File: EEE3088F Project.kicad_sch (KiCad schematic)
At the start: 69 parts, among them J1 Conn_02x16_Odd_Even, J2 Battery IN JST, M1Control1 DRV8837, M2Control1 DRV8837, M3Control1 DRV8837, M4Control1 DRV8837, Q2 AO3400A, U1 TP4056, U2 TPS62163DSG, U3 MT3608, U5 TPS62162DSG, U6 CH224K

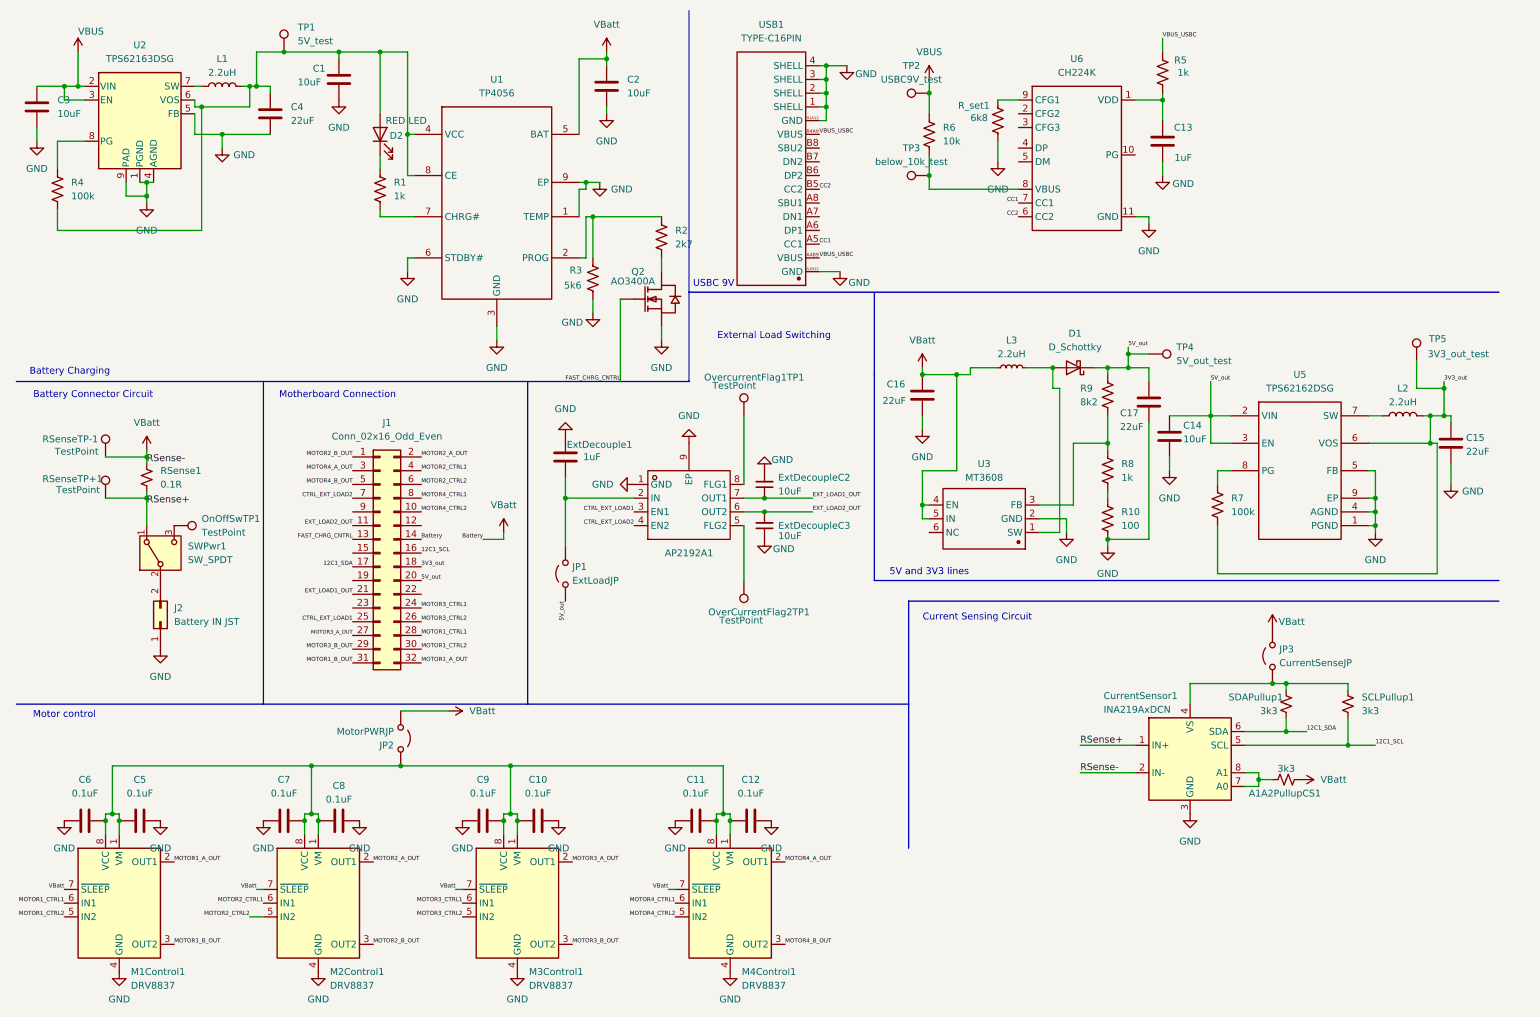
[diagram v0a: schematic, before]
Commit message: Fixed BOM
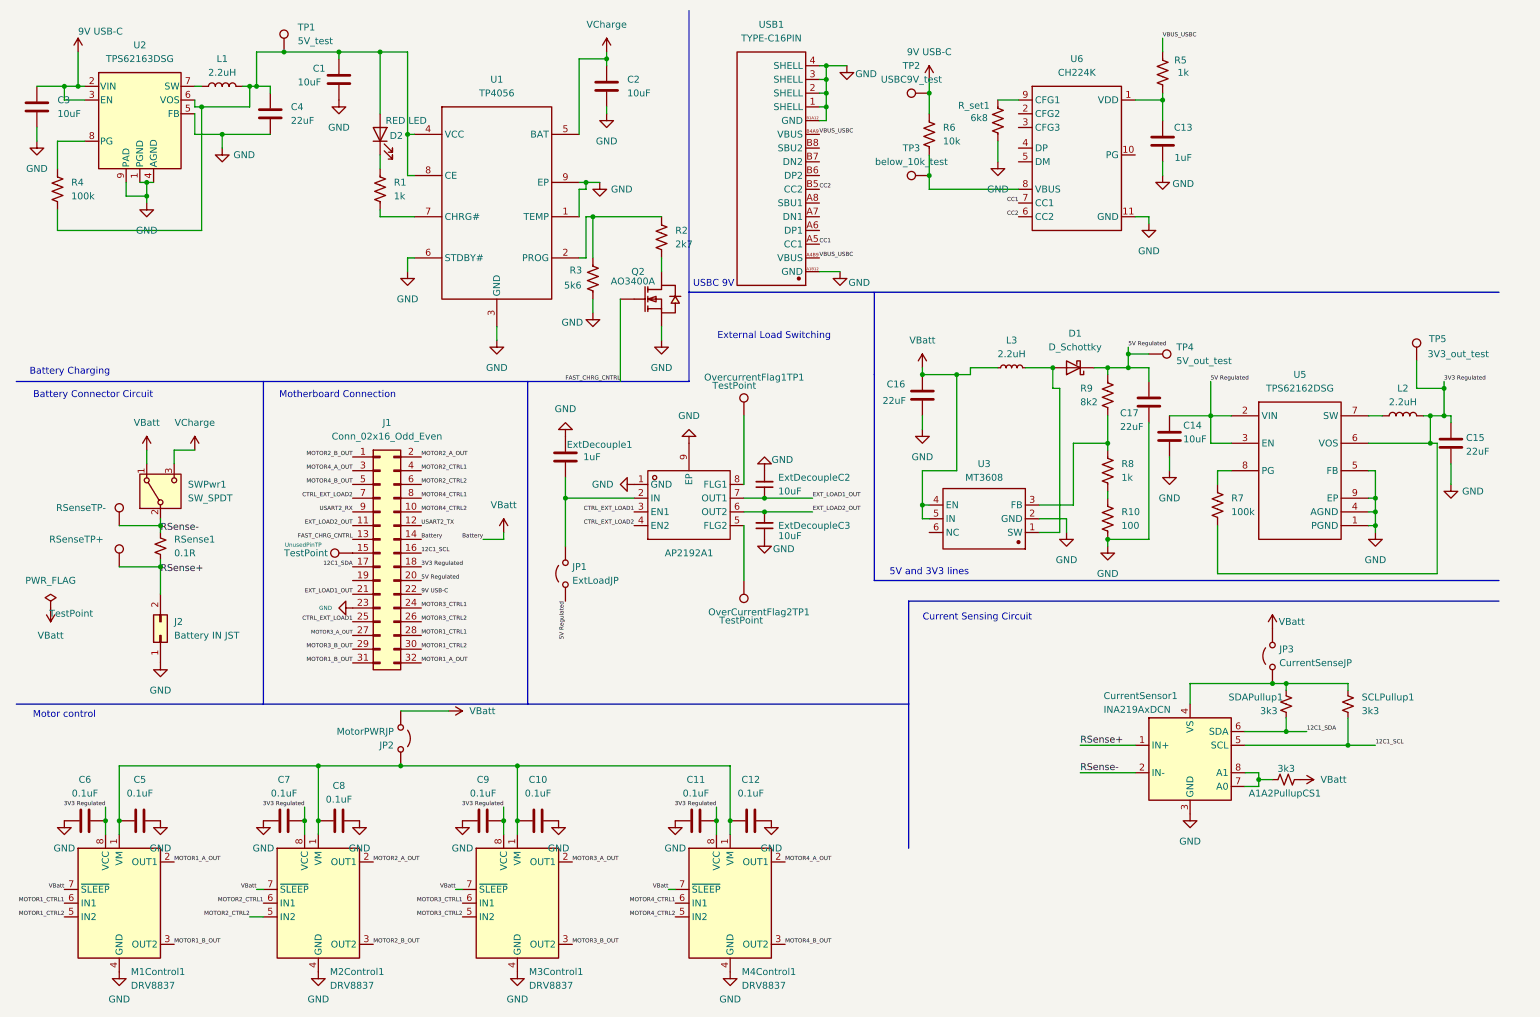
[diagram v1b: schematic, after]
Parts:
- removed OnOffSwTP1: TestPoint, symbol Connector:TestPoint
- added UnusedPinTP: TestPoint, symbol Connector:TestPoint
- renumbered RSenseTP+1 to RSenseTP+, RSenseTP-1 to RSenseTP-
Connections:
- net VBUS is gone; now on net 9V USB-C: C3.1, R6.1, TP2.1, U2.2 (VIN), U2.3 (EN)
- net GND: now also J1.23 (Pin_23)
- net RSense+: now also J2.2 (Pin_2); no longer SWPwr1.1 (A)
- net VBatt: now also SWPwr1.1 (A); no longer C2.1, CurrentSensor1.2 (IN-), RSense1.1, RSenseTP-.1, U1.5 (BAT)
- net USART2_TX: now reaches J1.12 (Pin_12)
- net at J1.15 (Pin_15): now also UnusedPinTP.1
- net 9V USB-C: now reaches J1.22 (Pin_22)
- net USART2_RX: now reaches J1.9 (Pin_9)
- net at C10.1, C12.1, C5.1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: no longer C11.2, C6.2, C7.2, C9.2, M1Control1.8 (VCC), M2Control1.8 (VCC), M3Control1.8 (VCC), M4Control1.8 (VCC)
- net VCharge: now reaches SWPwr1.3 (C)
- net VCharge: now also C2.1, U1.5 (BAT)
- net RSense-: now reaches SWPwr1.2 (B)
- net RSense-: now also CurrentSensor1.2 (IN-), RSense1.1, RSenseTP-.1; no longer J2.2 (Pin_2)
- net 3V3_out renamed 3V3 Regulated
- net 3V3 Regulated: now also C11.2, C6.2, C7.2, C9.2, M1Control1.8 (VCC), M2Control1.8 (VCC), M3Control1.8 (VCC), M4Control1.8 (VCC)
- net 5V_out renamed 5V Regulated
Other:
- moved on the sheet: J2, RSense1, RSenseTP+, RSenseTP-, SWPwr1

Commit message: changed inductors
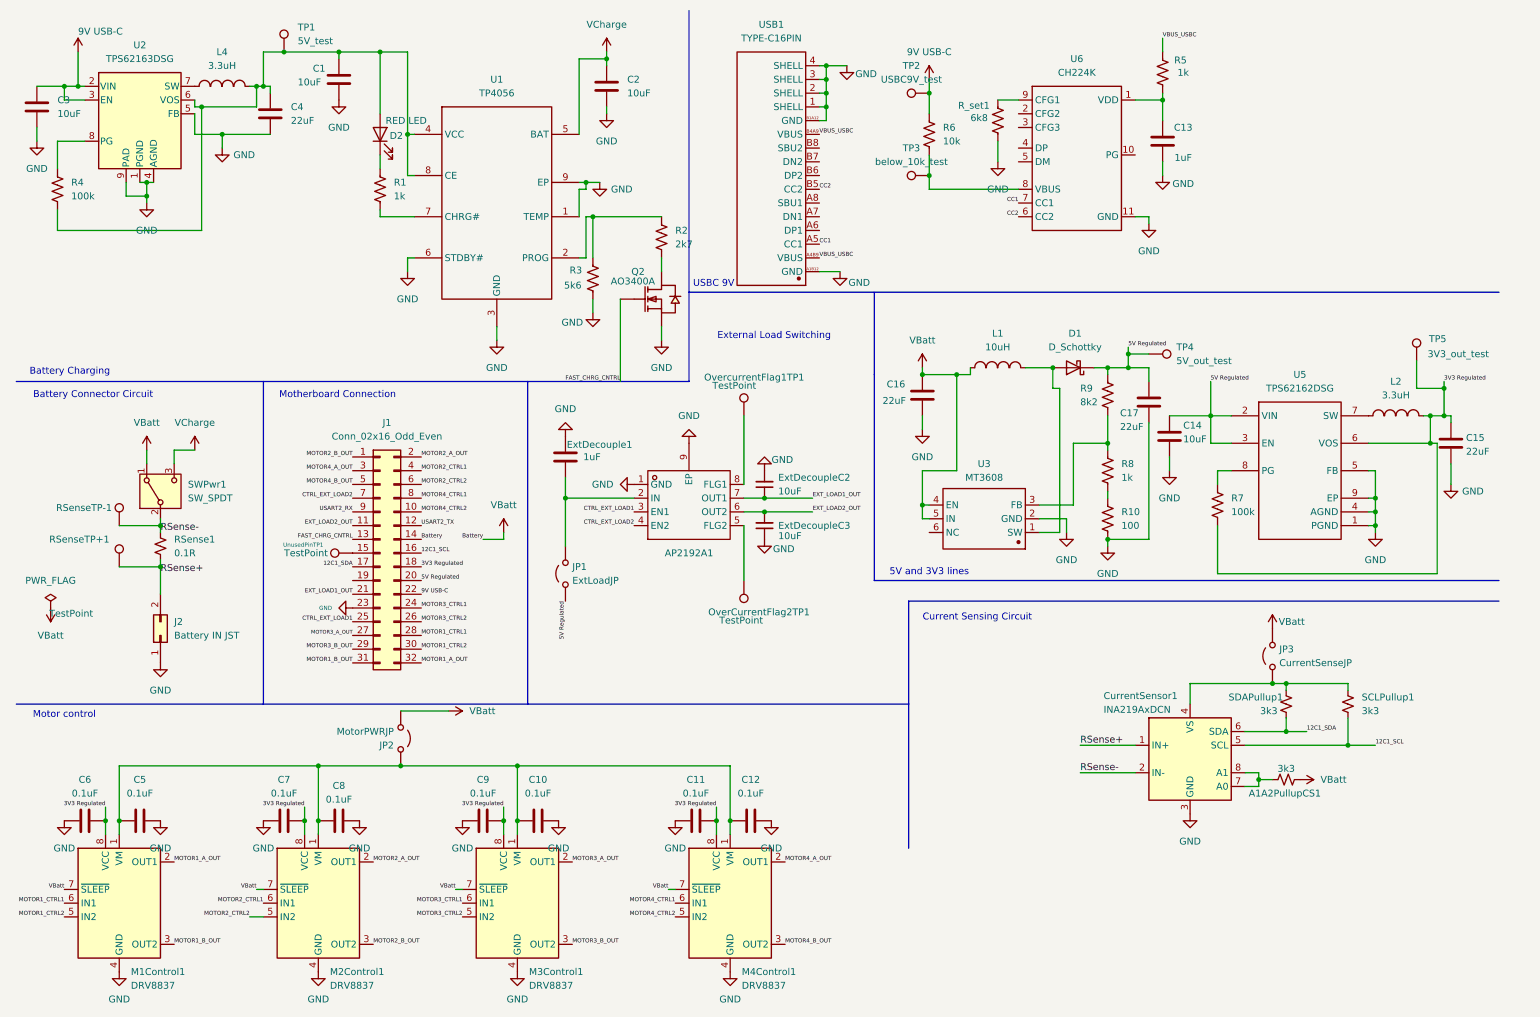
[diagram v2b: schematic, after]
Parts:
- removed L1, L2: 2.2uH, Inductor_SMD:L_Taiyo-Yuden_MD-3030, symbol Device:L
- removed L3: 2.2uH, Inductor_SMD:L_Taiyo-Yuden_MD-3030, symbol Device:L_Small
- added L1: 10uH, Custom Footprints:IND-SMD_L7.8-W7.0-A, symbol Custom Symbols:SM7850-100MT
- added L2, L4: 3.3uH, Custom Footprints:IND-SMD_L4.0-W4.0_FNR40XXS, symbol Custom Symbols:FNR4030S3R3MT
- OverCurrentFlag2TP1, OvercurrentFlag1TP1, TP1, TP2, TP3, TP4, TP5: footprint (none) -> TestPoint:TestPoint_Pad_2.0x2.0mm
- UnusedPinTP1: renamed from UnusedPinTP; footprint (none) -> TestPoint:TestPoint_Pad_2.0x2.0mm
- renumbered RSenseTP+ to RSenseTP+1, RSenseTP- to RSenseTP-1
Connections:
- net 3V3 Regulated: now also L2.2
- net VBatt: now also L1.1
- net at D1.2 (A), U3.1 (SW): now also L1.2
- net at C1.2, C4.1, D2.2 (A)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: now also L4.2
- net at U2.7 (SW): now also L4.1
- net at U5.7 (SW): now also L2.1

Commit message: Routed Thomas half of PCB traces. Minor labelling modifications in schematic.
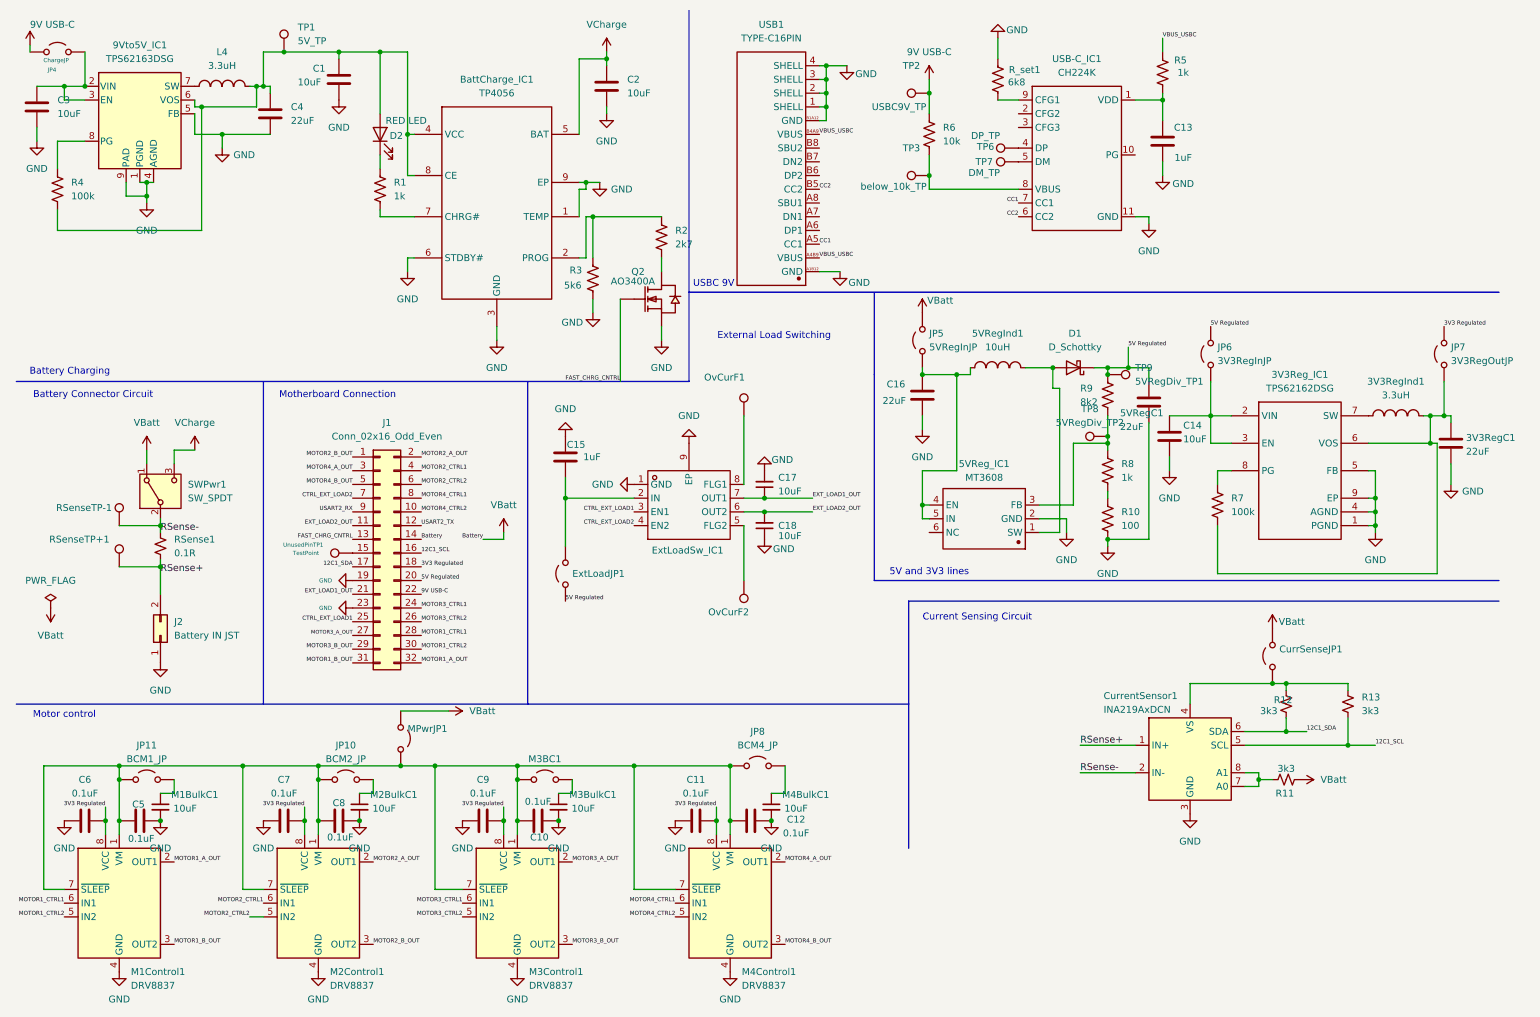
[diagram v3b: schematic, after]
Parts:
- removed TP4: 5V_out_test, TestPoint:TestPoint_Pad_2.0x2.0mm, symbol Connector:TestPoint
- removed TP5: 3V3_out_test, TestPoint:TestPoint_Pad_2.0x2.0mm, symbol Connector:TestPoint
- added JP10: BCM2_JP, Jumper:SolderJumper-2_P1.3mm_Open_Pad1.0x1.5mm, symbol Jumper:Jumper_2_Open
- added JP11: BCM1_JP, Jumper:SolderJumper-2_P1.3mm_Open_Pad1.0x1.5mm, symbol Jumper:Jumper_2_Open
- added JP4: ChargeJP, Jumper:SolderJumper-2_P1.3mm_Open_Pad1.0x1.5mm, symbol Jumper:Jumper_2_Open
- added JP5: 5VRegInJP, Jumper:SolderJumper-2_P1.3mm_Open_Pad1.0x1.5mm, symbol Jumper:Jumper_2_Open
- added JP6: 3V3RegInJP, Jumper:SolderJumper-2_P1.3mm_Open_Pad1.0x1.5mm, symbol Jumper:Jumper_2_Open
- added JP7: 3V3RegOutJP, Jumper:SolderJumper-2_P1.3mm_Open_Pad1.0x1.5mm, symbol Jumper:Jumper_2_Open
- added JP8: BCM4_JP, Jumper:SolderJumper-2_P1.3mm_Open_Pad1.0x1.5mm, symbol Jumper:Jumper_2_Open
- added M1BulkC1, M2BulkC1, M3BulkC1, M4BulkC1: 10uF, Capacitor_SMD:C_0805_2012Metric_Pad1.18x1.45mm_HandSolder, symbol Device:C_Small
- added M3BC1: BCM3_JP, Jumper:SolderJumper-2_P1.3mm_Open_Pad1.0x1.5mm, symbol Jumper:Jumper_2_Open
- added TP6: DP_TP, TestPoint:TestPoint_Pad_2.0x2.0mm, symbol Connector:TestPoint
- added TP7: DM_TP, TestPoint:TestPoint_Pad_2.0x2.0mm, symbol Connector:TestPoint
- added TP8: 5VRegDiv_TP2, TestPoint:TestPoint_Pad_2.0x2.0mm, symbol Connector:TestPoint
- added TP9: 5VRegDiv_TP1, TestPoint:TestPoint_Pad_2.0x2.0mm, symbol Connector:TestPoint
- CurrSenseJP1: renamed from JP3; footprint (none) -> Jumper:SolderJumper-2_P1.3mm_Open_Pad1.0x1.5mm
- ExtLoadJP1: renamed from JP1; footprint (none) -> Jumper:SolderJumper-2_P1.3mm_Open_Pad1.0x1.5mm
- MPwrJP1: renamed from JP2; footprint (none) -> Jumper:SolderJumper-2_P1.3mm_Open_Pad1.0x1.5mm
- TP1: value 5V_test -> 5V_TP
- TP2: value USBC9V_test -> USBC9V_TP
- TP3: value below_10k_test -> below_10k_TP
- renumbered C15 to 3V3RegC1, L2 to 3V3RegInd1, U5 to 3V3Reg_IC1, C17 to 5VRegC1, L1 to 5VRegInd1, U3 to 5VReg_IC1, U2 to 9Vto5V_IC1, U1 to BattCharge_IC1, ExtDecouple1 to C15, ExtDecoupleC2 to C17, ExtDecoupleC3 to C18, AP2192A1 to ExtLoadSw_IC1, OvercurrentFlag1TP1 to OvCurF1, OverCurrentFlag2TP1 to OvCurF2, A1A2PullupCS1 to R11, SDAPullup1 to R12, SCLPullup1 to R13, U6 to USB-C_IC1
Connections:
- net MOTOR2_B_OUT is gone; now on net MOTOR2_B_OUT : J1.1 (Pin_1)
- net MOTOR2_CTRL2  is gone; now on net MOTOR2_CTRL2: J1.6 (Pin_6)
- net MOTOR4_B_OUT  is gone; now on net MOTOR4_B_OUT: M4Control1.3 (OUT2)
- net MOTOR4_CTRL1  is gone; now on net MOTOR4_CTRL1: J1.8 (Pin_8)
- net 3V3 Regulated: now also JP7.2 (B); no longer 3V3RegC1.1, 3V3RegInd1.2, 3V3Reg_IC1.6 (VOS), R7.2
- net 5V Regulated: now also JP6.2 (B), TP9.1; no longer 3V3Reg_IC1.2 (VIN), 3V3Reg_IC1.3 (EN), C14.1
- net 9V USB-C: now also JP4.1 (A); no longer 9Vto5V_IC1.2 (VIN), 9Vto5V_IC1.3 (EN), C3.1
- net GND: now also J1.19 (Pin_19), M1BulkC1.2, M2BulkC1.2, M3BulkC1.2, M4BulkC1.2
- net VBatt: now also JP5.2 (B); no longer 5VRegInd1.1, 5VReg_IC1.4 (EN), 5VReg_IC1.5 (IN), C16.1, M1Control1.7 (~{SLEEP}), M2Control1.7 (~{SLEEP}), M3Control1.7 (~{SLEEP}), M4Control1.7 (~{SLEEP})
- net at C10.1, C12.1, C5.1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: now also M1Control1.7 (~{SLEEP}), M2Control1.7 (~{SLEEP}), M3Control1.7 (~{SLEEP}), M4Control1.7 (~{SLEEP}), JP10.1 (A), JP11.1 (A), JP8.1 (A), M3BC1.1 (A)
- net at USB-C_IC1.4 (DP): now also TP6.1
- net at USB-C_IC1.5 (DM): now also TP7.1
- net at 5VReg_IC1.3 (FB), R8.1, R9.2: now also TP8.1
- new net: 9Vto5V_IC1.2 (VIN), 9Vto5V_IC1.3 (EN), C3.1, JP4.2 (B)
- new net: 3V3RegC1.1, 3V3RegInd1.2, 3V3Reg_IC1.6 (VOS), JP7.1 (A), R7.2
- new net: JP8.2 (B), M4BulkC1.1
- new net: 5VRegInd1.1, 5VReg_IC1.4 (EN), 5VReg_IC1.5 (IN), C16.1, JP5.1 (A)
- new net: JP10.2 (B), M2BulkC1.1
- new net: M3BC1.2 (B), M3BulkC1.1
- new net: 3V3Reg_IC1.2 (VIN), 3V3Reg_IC1.3 (EN), C14.1, JP6.1 (A)
- new net: JP11.2 (B), M1BulkC1.1
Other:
- moved on the sheet: R_set1
